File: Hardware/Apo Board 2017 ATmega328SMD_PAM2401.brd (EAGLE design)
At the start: 85.1 x 52.7 mm, 40 parts, among them Q1 RESONATORSMD, U1 LED-TRICOLOR-5050-IC, U10 LED-TRICOLOR-5050-IC, U11 LED-TRICOLOR-5050-IC, U13 ATMEGA328, U2 PAM2401, U3 LED-TRICOLOR-5050-IC, U4 LED-TRICOLOR-5050-IC, U5 LED-TRICOLOR-5050-IC, U6 LED-TRICOLOR-5050-IC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

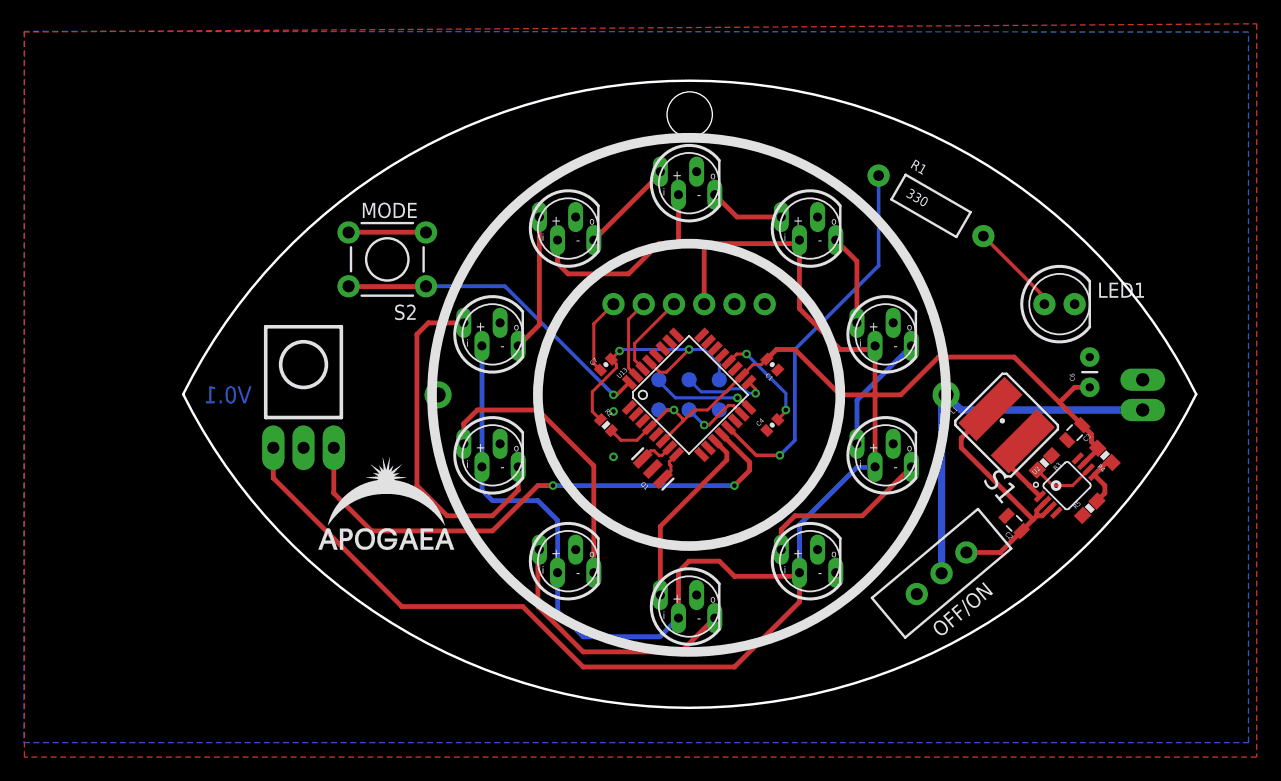
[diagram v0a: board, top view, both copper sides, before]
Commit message: increased +5v trace width, moved all power traces to top layer, added a fair amount of sitching vias
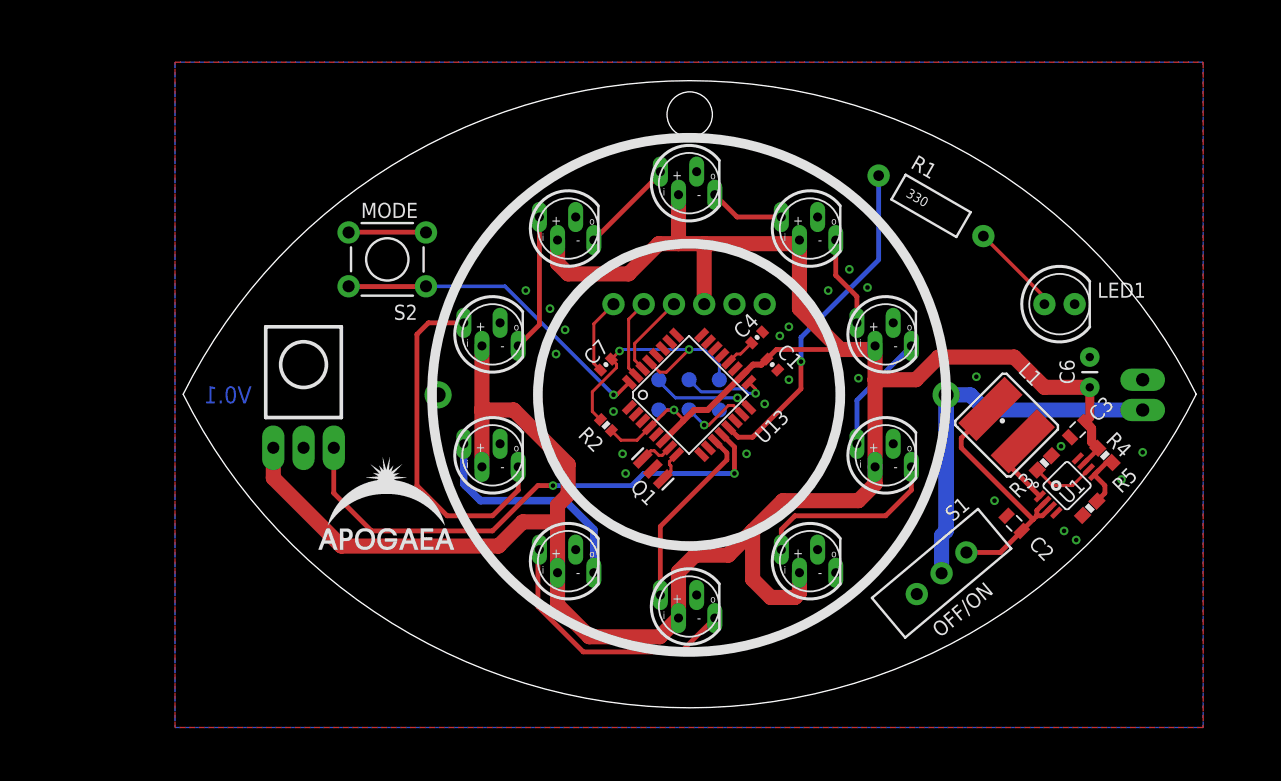
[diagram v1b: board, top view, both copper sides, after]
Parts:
- U1: value LED-TRICOLOR-5050-IC -> PAM2401; device SparkFun-LED:LED-RGB-THRU -> SparkFun-PowerIC:MSOP8
- U2: value PAM2401 -> LED-TRICOLOR-5050-IC; device SparkFun-PowerIC:MSOP8 -> SparkFun-LED:LED-RGB-THRU
- moved U1 15.5 mm to (31.8, -7.62), turned to 315 degrees
- moved U2 15.5 mm to (16.5, -5.08), turned to 180 degrees
- moved C4 7.47 mm to (5.71, 4.83), turned to 225 degrees
- moved C3 0.36 mm to (32.6, -2.92)
- renumbered JP1 to U12
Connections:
- net N$7 renamed +BATT_RAW
- net +5V: now also U1.7, U2.2; no longer U1.2, U2.7
- net GND: now also U1.4, U1.8, U2.3; no longer U1.3, U2.4, U2.8
- net N$10: now also U1.2, U1.3; no longer U2.2, U2.3
- net N$12: now also U1.5; no longer U2.5
- net N$13: now also U2.1; no longer U1.1
- net N$14: now also U2.4; no longer U1.4
- net N$4: now also U1.6; no longer U2.6
- net N$8: now also U1.1; no longer U2.1
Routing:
- net +5V: track 252.0 -> 219.8 mm
- net +BATT_RAW: track 32.2 -> 43.6 mm
- net AREF: track 8.95 -> 2.61 mm, vias 2 -> 0
- net N$2: track 24.0 -> 19.5 mm
- net IR_TX: track 32.2 -> 28.7 mm
- net IR_RX: track 46.2 -> 44.5 mm
- net N$14: track 14.8 -> 15.9 mm
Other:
- board text added: "3) Press button to share mode"
- board text added: "4) Collect as many modes as you can"
- board text added: "How to Play: 1) Two Eyeballs see one another 2) LEDs start pulsing"
- board text removed: "3)Press button to share mode"
- board text removed: "4)Collect as many modes as you can"
- board text removed: "How to Play: 1)Two Eyeballs see one another 2)LEDs start pulsing"
